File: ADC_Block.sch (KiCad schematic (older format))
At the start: 19 parts

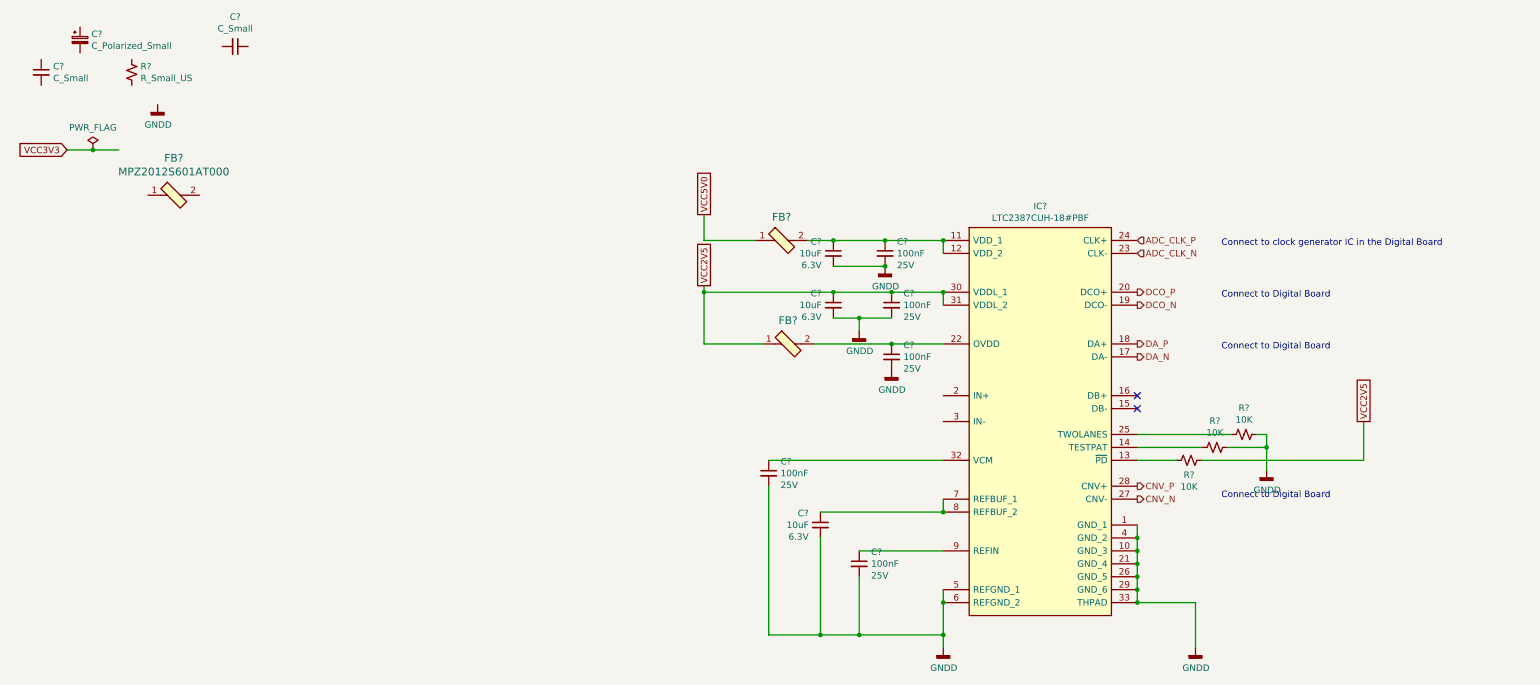
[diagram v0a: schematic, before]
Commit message: PCB created and schematics annotated High speed connections added to the BTB
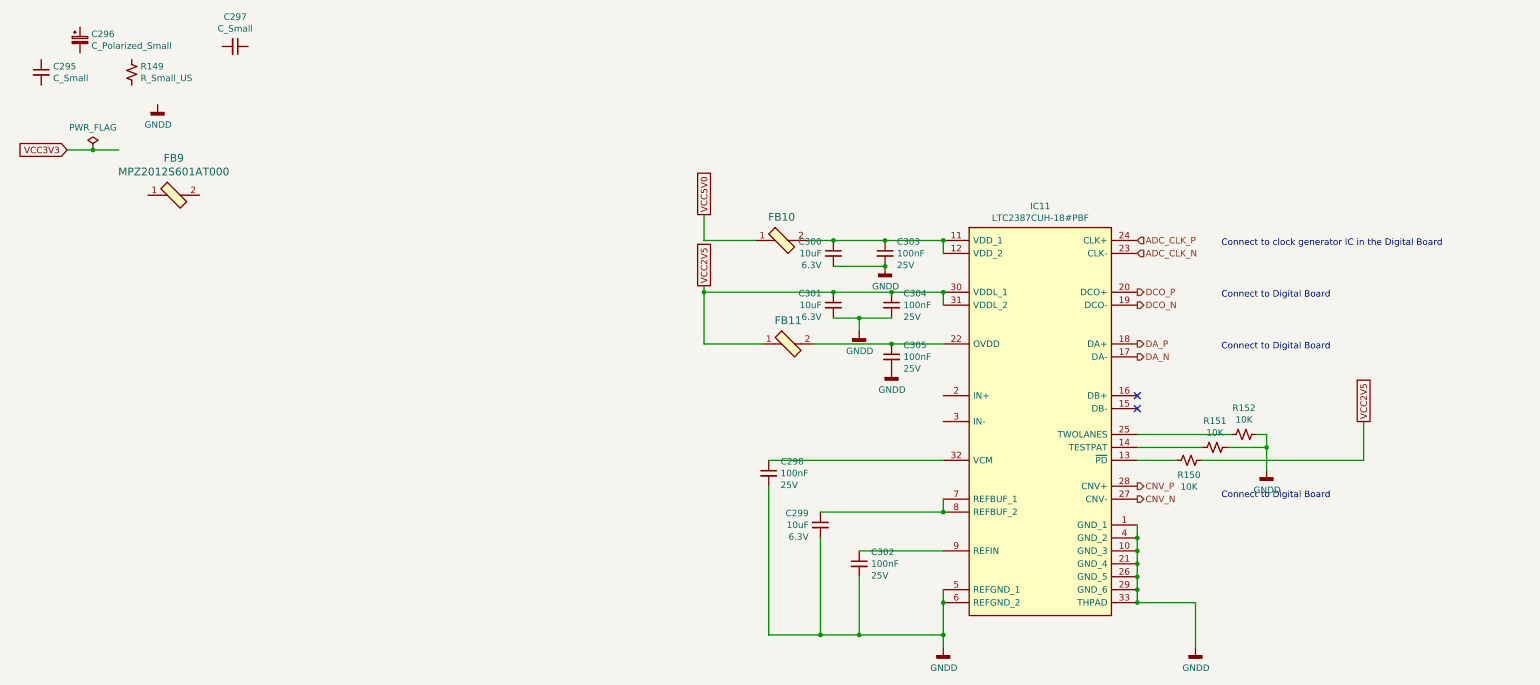
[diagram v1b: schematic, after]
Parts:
- gave numbers to parts that had none: 19

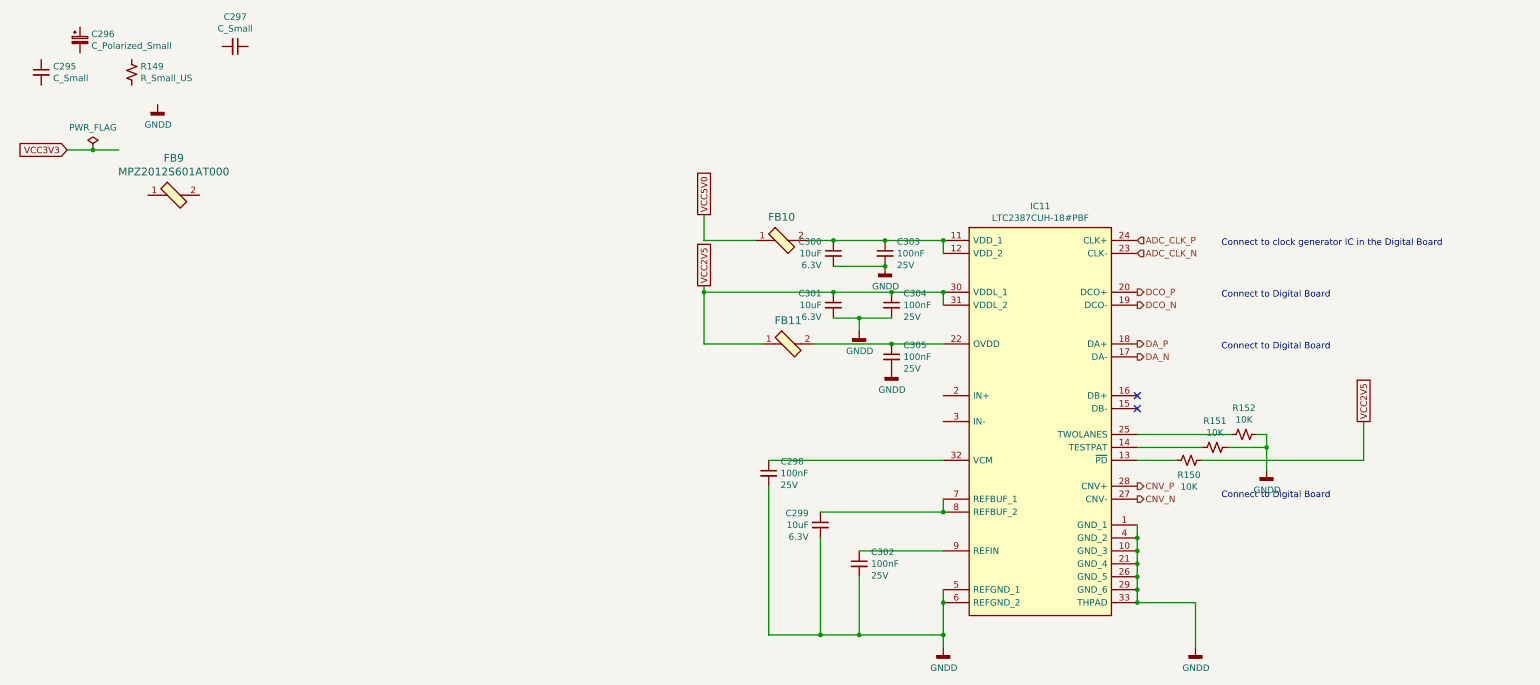
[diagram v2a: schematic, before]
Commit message: Corrected PCB import errors
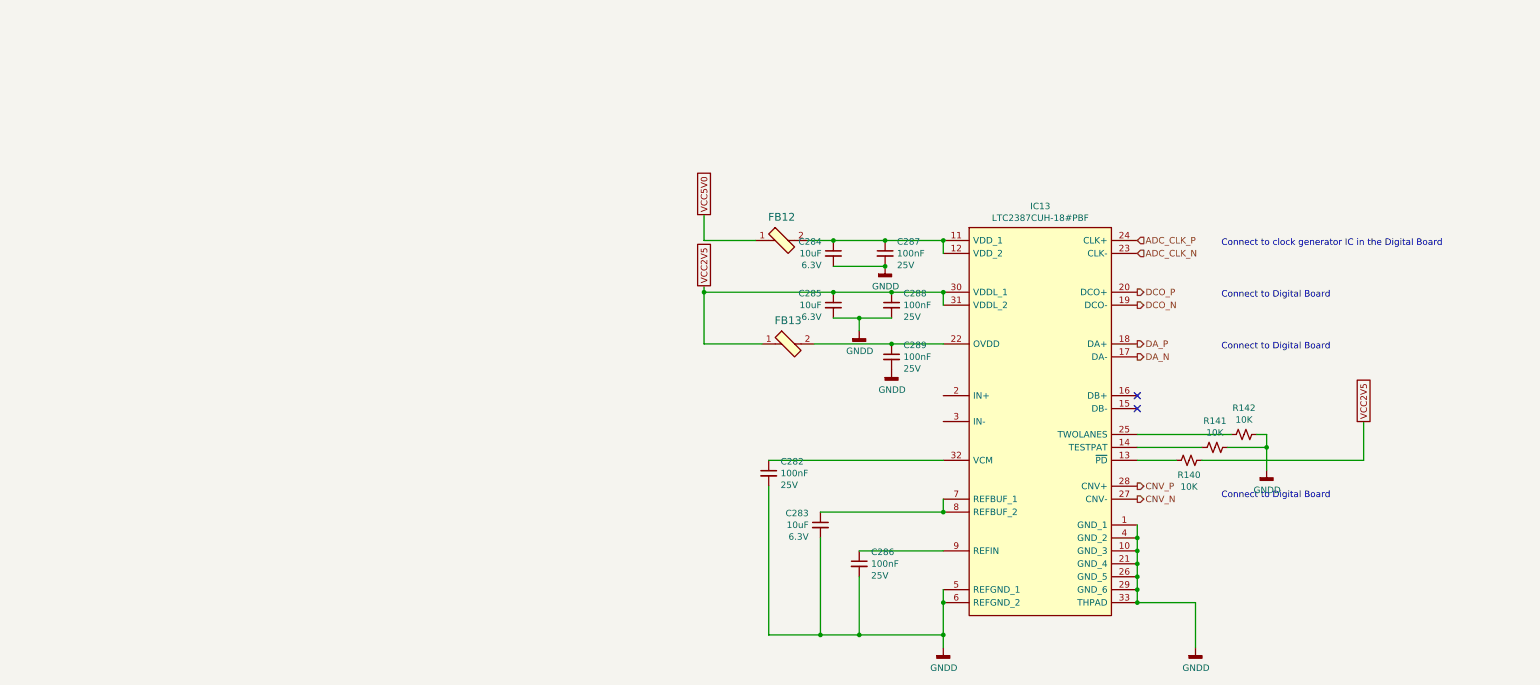
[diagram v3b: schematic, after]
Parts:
- removed C295: C_Small, Capacitor_SMD:C_0603_1608Metric_Pad1.08x0.95mm_HandSolder, symbol Device:C_Small
- removed C296: C_Polarized_Small, Capacitor_Tantalum_SMD:CP_EIA-1608-10_AVX-L_Pad1.25x1.05mm_HandSolder, symbol Device:C_Polarized_Small
- removed C297: C_Small, symbol Device:C_Small
- removed FB9: MPZ2012S601AT000, digikey-footprints:0805, symbol dk_Ferrite-Beads-and-Chips:MPZ2012S601AT000
- removed R149: R_Small_US, Resistor_SMD:R_0603_1608Metric_Pad0.98x0.95mm_HandSolder, symbol Device:R_Small_US
- renumbered C298 to C266, C299 to C267, C300 to C268, C301 to C269, C302 to C270, C303 to C271, C304 to C272, C305 to C273, FB10 to FB8, FB11 to FB9, R150 to R134, R151 to R135, R152 to R136
